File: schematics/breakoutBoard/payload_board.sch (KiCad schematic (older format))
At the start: 10 parts, among them J1 Power_Breakout, J2 MIO_Breakout, J3 USB_OTG_Breakout, J4 Cardedge breakout, P1 CONN_02X50, P2 CONN_02X50, P3 CONN_02X50, P4 CONN_02X50, P5 CONN_02X30, P7 CONN_02X30

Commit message: Fixed gerber files
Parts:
- J1: symbol Conn_01x10 -> conn:Conn_01x10
- J2: symbol Conn_01x12 -> conn:Conn_01x12
- J3: symbol Conn_02x03_Counter_Clockwise -> conn:Conn_02x03_Counter_Clockwise
- J4: symbol Conn_01x17 -> conn:Conn_01x17
- P1, P2, P3, P4: symbol CONN_02X50 -> payload_board-rescue:CONN_02X50
- P5, P7: symbol Conn_02x30_Odd_Even -> conn:Conn_02x30_Odd_Even
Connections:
- wire segments 439 -> 822

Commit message: completed layout w/o impedance matching
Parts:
- removed J1: Power_Breakout, Pin_Headers:Pin_Header_Straight_1x10_Pitch2.54mm, symbol conn:Conn_01x10
- removed J2: MIO_Breakout, Pin_Headers:Pin_Header_Straight_1x12_Pitch2.54mm, symbol conn:Conn_01x12
- removed J3: USB_OTG_Breakout, Pin_Headers:Pin_Header_Straight_1x06_Pitch2.54mm, symbol conn:Conn_02x03_Counter_Clockwise
- removed J4: Cardedge breakout, Pin_Headers:Pin_Header_Straight_1x17_Pitch2.54mm, symbol conn:Conn_01x17
- removed P5: CONN_02X30, Connectors_Samtec:MECF-30-01-L-DV-WT_Socket, symbol conn:Conn_02x30_Odd_Even
- removed P7: CONN_02X30, Connectors_Samtec:MECF-30-0_-NP-L-DV_Edge, symbol conn:Conn_02x30_Odd_Even
- added RIB1: B5B-EH-A, breakoutBoard:B5B-EH-A, symbol payload_board-rescue:B5B-EH-A
- added SMA1: Molex-MMCX-SMD, breakoutBoard:Molex MMCX SMD 50Ohm, symbol payload_board-rescue:Molex-MMCX-SMD
- added U1: breakout_carrier, breakoutBoard:breakout_carrier, symbol payload_board-rescue:breakout_carrier
- P1, P2, P3, P4: footprint Project:BERGSTAK_100_PIN1_RIGHT -> breakoutBoard:BERGSTAK_100_PIN1_RIGHT
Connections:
- net labels removed: +5V, 3V3_I2C, AD9361_GPO_VDD, AUXADC, AUXDAC1, AUXDAC2, Carrier_Reset, FPGA_DONE, FPGA_VBATT, GND, GPO_0, GPO_1, GPO_2, GPO_3, IO_00_33_JX1, IO_L01_33_JX1_N, IO_L01_33_JX1_P, IO_L16_33_JX1_N, IO_L16_33_JX1_P, IO_L18_33_JX1_N, IO_L18_33_JX1_P, IO_L20_33_JX1_N, IO_L20_33_JX1_P, IO_L22_33_JX1_N, IO_L22_33_JX1_P, JTAG_TCK, JTAG_TDI, JTAG_TDO, JTAG_TMS, JX_MGTAVCC, JX_MGTAVTT, JX_VCCO_12, JX_VCCO_13, JX_VCCO_33_34, MIO0, MIO10, MIO11, MIO12, MIO13, MIO14, MIO15, MIO46, MIO47, MIO48, MIO49, MIO51, PG_1P8V, PG_MODULE, PWR_ENABLE, USB_ID, USB_OTG_CPEN, USB_OTG_N, USB_OTG_P, USB_VBUS_OTG, VCCO_13, VDDA_GPO_PWR
- wire segments 822 -> 48
- no-connect marks 4 -> 0
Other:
- note removed: "<-Might need to remove"
- note removed: "JX1\n"
- note removed: "JX2\n"
- note removed: "JX3"
- note removed: "JX4"

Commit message: 'final' push
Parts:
- removed RIB1: B5B-EH-A, breakoutBoard:B5B-EH-A, symbol payload_board-rescue:B5B-EH-A
- added SMA2: Molex-MMCX-SMD, breakoutBoard:Molex MMCX SMD 50Ohm, symbol payload_board-rescue:Molex-MMCX-SMD
- added e1: ribbon2.54mmPitch, breakoutBoard:ribbon2.5mmPitch, symbol payload_board-rescue:ribbon2.54mmPitch
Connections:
- net at P2.17 (P17), U1.1 (SDR_EN): now also e1.2 (I2C_SCL)
- net at P2.19 (P19), U1.2 (UART_TX): now also e1.3 (I2C_SDA)
- net at P1.5 (P5), U1.3 (UART_RX): now also e1.4 (SDR_EN)
- net at P1.57 (P57), P1.58 (P58), P1.59 (P59)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: now also e1.1 (PWR)
- net at P3.11 (P11): now also P1.78 (P78), P1.79 (P79), P1.80 (P80), P1.95 (P95), P2.78 (P78), P2.79 (P79), P2.80 (P80), P2.98 (P98), P3.30 (P30), P3.32 (P32), P3.45 (P45), P3.46 (P46), P3.5 (P5), P3.7 (P7), P3.9 (P9), e1.5 (GND)
- net at P1.92 (P92): no longer SMA1.1 (RF_DIFF+)
- net at P1.94 (P94): no longer SMA1.2 (RF_DIFF-)
- net at P4.98 (P98): now also e1.6 (UART_TX)
- net at P4.99 (P99): now also e1.7 (UART_RX)
- new net: SMA1.1 (RF_DIFF+), SMA2.1 (RF_DIFF+)
- new net: SMA1.2 (RF_DIFF-), SMA2.2 (RF_DIFF-)
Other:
- moved on the sheet: SMA1
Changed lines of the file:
@@
-	1    0    0    -1
-$EndComp
-$Comp
-L payload_board-rescue:B5B-EH-A RIB1
-U 1 1 5CCD2E38
-P 2800 7150
-F 0 "RIB1" H 3078 7079 50  0000 L CNN
-F 1 "B5B-EH-A" H 3078 6988 50  0000 L CNN
-F 2 "breakoutBoard:B5B-EH-A" H 3078 6897 50  0000 L CNN
-F 3 "" H 2750 7250 50  0001 C CNN
-	1    2800 7150
 	1    0    0    -1
 $EndComp
@@
 L payload_board-rescue:Molex-MMCX-SMD SMA1
 U 1 1 5CCDD268
-P 2350 5850
-F 0 "SMA1" H 2428 5713 50  0000 L CNN
-F 1 "Molex-MMCX-SMD" H 2350 6100 50  0001 C CNN
-F 2 "breakoutBoard:Molex MMCX SMD 50Ohm" H 2350 5850 50  0001 C CNN
-F 3 "" H 2350 5850 50  0001 C CNN
-	1    2350 5850
+P 4950 7100
+F 0 "SMA1" H 5028 6963 50  0000 L CNN
+F 1 "Molex-MMCX-SMD" H 4950 7350 50  0001 C CNN
+F 2 "breakoutBoard:Molex MMCX SMD 50Ohm" H 4950 7100 50  0001 C CNN
+F 3 "" H 4950 7100 50  0001 C CNN
+	1    4950 7100
 	0    -1   1    0
 $EndComp
 Wire Wire Line
-	2250 5850 2050 5850
-Wire Wire Line
-	2250 5950 2050 5950
-Wire Wire Line
 	2950 7050 2950 6400
 Wire Wire Line
@@
 Wire Wire Line
 	1400 6400 2950 6400
+Wire Wire Line
+	2200 5150 2050 5150
+Wire Wire Line
+	2050 5250 2200 5250
+Wire Wire Line
+	2200 5250 2200 5150
+Wire Wire Line
+	1550 5250 1250 5250
+Wire Wire Line
+	1250 5250 1250 7550
+Wire Wire Line
+	1250 7550 3250 7550
+Wire Wire Line
+	3250 7550 3250 6400
+Wire Wire Line
+	3250 6400 3100 6400
+Connection ~ 2950 6400
+Wire Wire Line
+	3250 6400 3250 5350
+Wire Wire Line
+	3250 5350 3950 5350
+Connection ~ 3250 6400
+Wire Wire Line
+	4650 5250 5050 5250
+Wire Wire Line
+	5050 5250 5050 5350
+Wire Wire Line
+	5050 6600 3950 6600
+Wire Wire Line
+	3950 6600 3950 5350
+Connection ~ 3950 5350
+Wire Wire Line
+	3950 5350 4150 5350
+Wire Wire Line
+	4650 5350 5050 5350
+Connection ~ 5050 5350
+Wire Wire Line
+	5050 5350 5050 6250
+Wire Wire Line
+	4650 6250 5050 6250
+Connection ~ 5050 6250
+Wire Wire Line
+	5050 6250 5050 6600
+Wire Wire Line
+	7650 3300 7900 3300
+Wire Wire Line
+	7900 3300 7900 3750
+Wire Wire Line
+	7900 3750 6950 3750
+Wire Wire Line
+	5050 3750 5050 5250
+Connection ~ 5050 5250
+Wire Wire Line
+	7150 3300 6950 3300
+Connection ~ 6950 3750
+Wire Wire Line
+	6950 3750 5050 3750
+Wire Wire Line
+	7650 2500 7900 2500
+Wire Wire Line
+	7900 2500 7900 2600
+Connection ~ 7900 3300
+Wire Wire Line
+	7650 2600 7900 2600
+Connection ~ 7900 2600
+Wire Wire Line
+	7900 2600 7900 3300
+Wire Wire Line
+	7150 1300 6950 1300
+Wire Wire Line
+	6950 1300 6950 1400
+Connection ~ 6950 3300
+Wire Wire Line
+	6950 3300 6950 3750
+Wire Wire Line
+	7150 1400 6950 1400
+Connection ~ 6950 1400
+Wire Wire Line
+	6950 1400 6950 1500
+Wire Wire Line
+	7150 1500 6950 1500
+Connection ~ 6950 1500
+Wire Wire Line
+	6950 1500 6950 1600
+Wire Wire Line
+	7150 1600 6950 1600
+Connection ~ 6950 1600
+Wire Wire Line
+	6950 1600 6950 3300
+Wire Wire Line
+	2200 5150 3100 5150
+Wire Wire Line
+	3100 5150 3100 6400
+Connection ~ 2200 5150
+Connection ~ 3100 6400
+Wire Wire Line
+	3100 6400 2950 6400
+$Comp
+L payload_board-rescue:ribbon2.54mmPitch e1
+U 1 1 5CCBC1CC
+P 2700 7250
+F 0 "e1" H 3150 7250 50  0001 C CNN
+F 1 "ribbon2.54mmPitch" H 3228 7213 50  0000 L CNN
+F 2 "breakoutBoard:ribbon2.5mmPitch" H 3150 7250 50  0001 C CNN
+F 3 "" H 3150 7250 50  0001 C CNN
+	1    2700 7250
+	1    0    0    -1
+$EndComp
+$Comp
+L payload_board-rescue:Molex-MMCX-SMD SMA2
+U 1 1 5CCBDC56
+P 4550 7100
+F 0 "SMA2" H 4628 6963 50  0000 L CNN
+F 1 "Molex-MMCX-SMD" H 4550 7350 50  0001 C CNN
+F 2 "breakoutBoard:Molex MMCX SMD 50Ohm" H 4550 7100 50  0001 C CNN
+F 3 "" H 4550 7100 50  0001 C CNN
+	1    4550 7100
+	0    1    1    0
+$EndComp
+Wire Wire Line
+	4650 7100 4850 7100
+Wire Wire Line
+	4850 7200 4650 7200
+Wire Wire Line
+	9750 6300 10300 6300
+Wire Wire Line
+	10300 6300 10300 6700
+Wire Wire Line
+	10300 6700 3050 6700
+Wire Wire Line
+	3050 6700 3050 7050
+Wire Wire Line
+	3150 7050 3400 7050
+Wire Wire Line
+	4200 7050 4200 6850
+Wire Wire Line
+	4200 6850 9100 6850
+Wire Wire Line
+	9100 6850 9100 6400
+Wire Wire Line
+	9100 6400 9250 6400
+Wire Wire Line
+	2150 7250 2400 7250
+Wire Wire Line
+	2400 7250 2400 6700
+Wire Wire Line
+	2400 6700 3050 6700
+Connection ~ 3050 6700
+Wire Wire Line
+	3400 7050 3400 7400
+Wire Wire Line
+	3400 7400 2150 7400
+Connection ~ 3400 7050
+Wire Wire Line
+	3400 7050 4200 7050
 $EndSCHEMATC

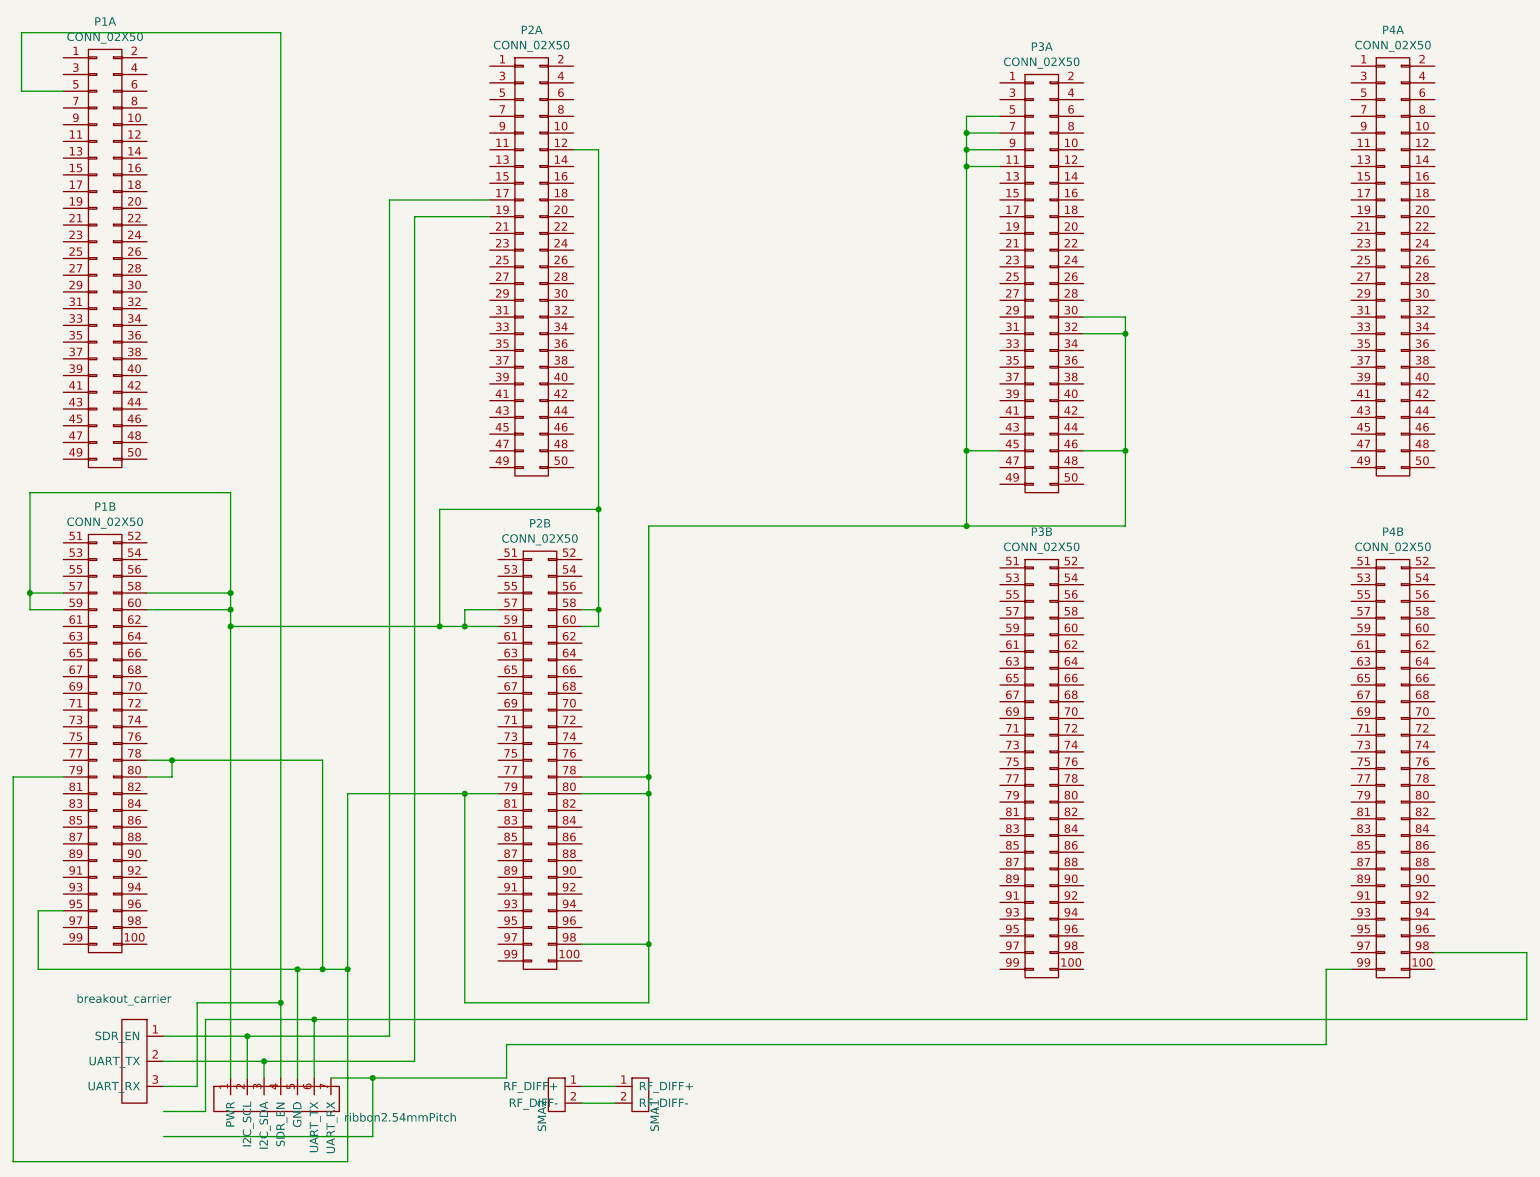
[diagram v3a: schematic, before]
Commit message: final board v2, now with UART
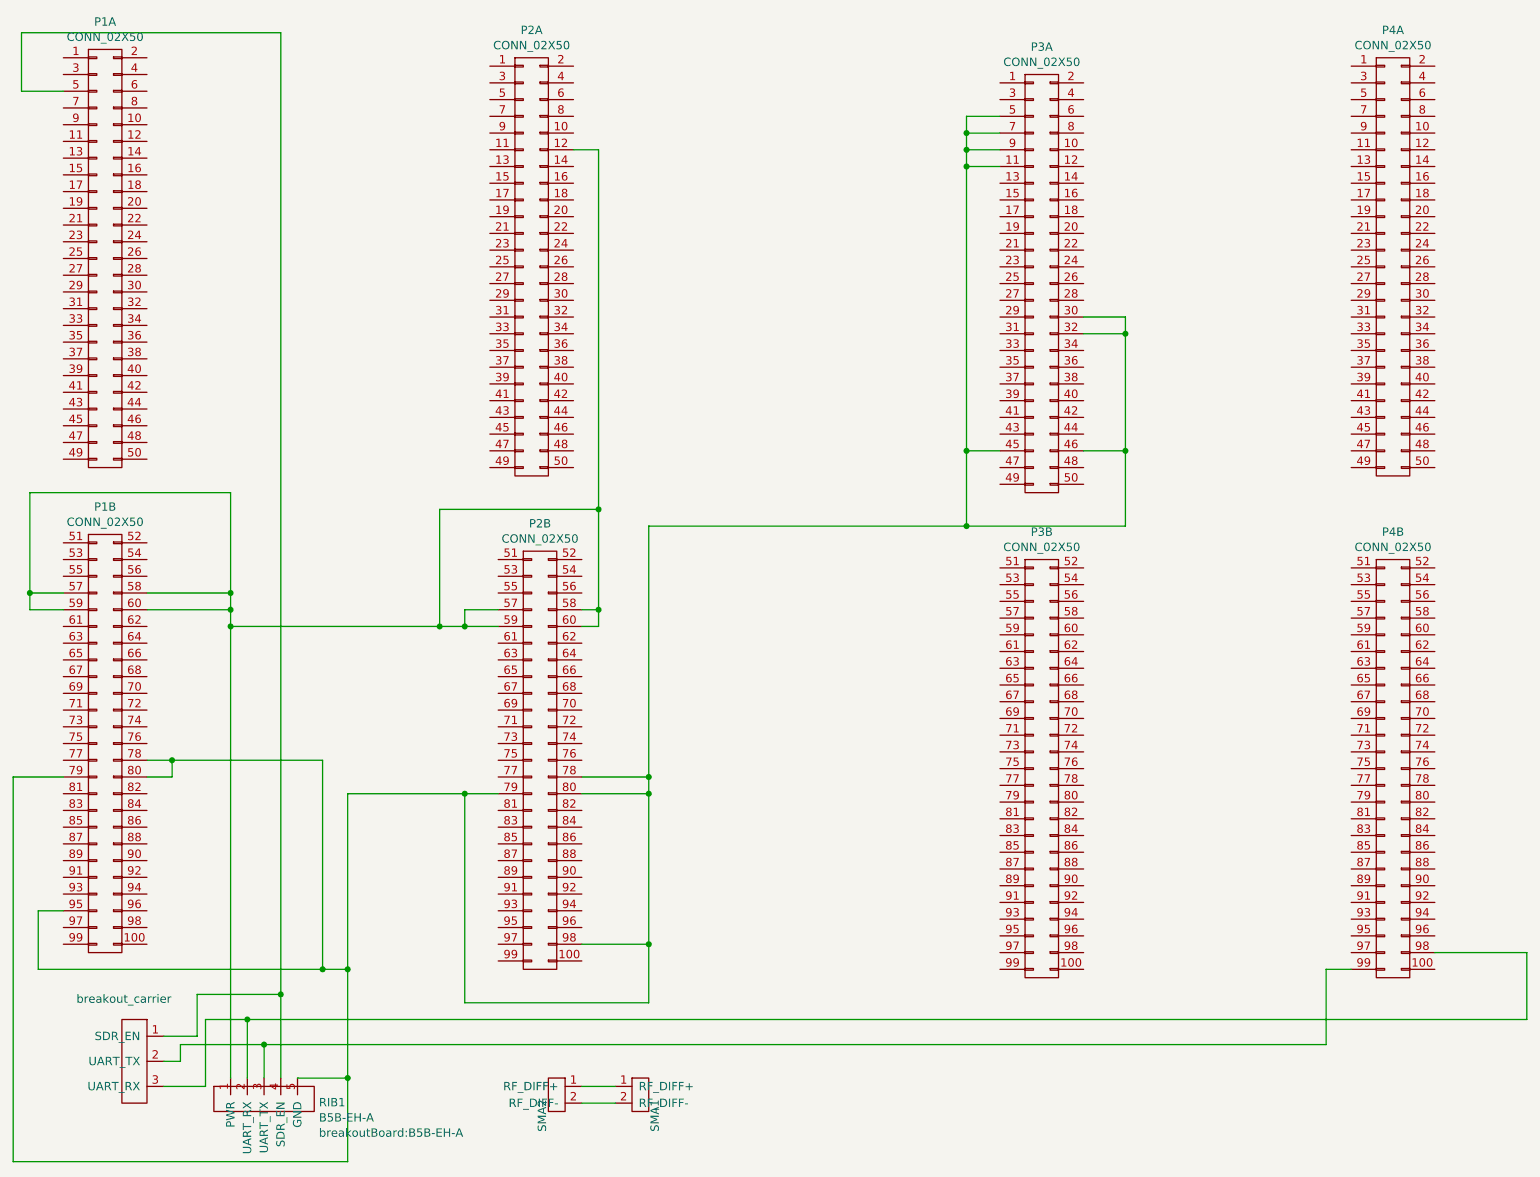
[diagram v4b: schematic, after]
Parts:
- removed e1: ribbon2.54mmPitch, breakoutBoard:ribbon2.5mmPitch, symbol payload_board-rescue:ribbon2.54mmPitch
- added RIB1: B5B-EH-A, breakoutBoard:B5B-EH-A, symbol payload_board-rescue:B5B-EH-A
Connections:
- net at U1.1 (SDR_EN): now also P1.5 (P5), RIB1.4 (SDR_EN); no longer P2.17 (P17)
- net at U1.2 (UART_TX): now also P4.99 (P99), RIB1.3 (UART_TX); no longer P2.19 (P19)
- net at U1.3 (UART_RX): now also P4.98 (P98), RIB1.2 (UART_RX); no longer P1.5 (P5)
- net at P1.57 (P57), P1.58 (P58), P1.59 (P59)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: now also RIB1.1 (PWR)
- net at P1.78 (P78), P1.79 (P79), P1.80 (P80)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: now also RIB1.5 (GND)
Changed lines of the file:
@@
 Wire Wire Line
 	1300 1150 1550 1150
-Wire Wire Line
-	4100 1900 3650 1900
-Wire Wire Line
-	2650 6800 3500 6800
-Wire Wire Line
-	2750 7050 2750 6950
-Wire Wire Line
-	3500 1800 4100 1800
-Wire Wire Line
-	3500 1800 3500 6800
-Wire Wire Line
-	2750 6950 3650 6950
-Wire Wire Line
-	3650 1900 3650 6950
-Wire Wire Line
-	2650 6800 2650 7050
-Wire Wire Line
-	2850 800  2850 6600
 $Comp
 L payload_board-rescue:breakout_carrier U1
@@
 $EndComp
 Wire Wire Line
-	2150 6800 2650 6800
-Connection ~ 2650 6800
-Wire Wire Line
-	2150 6950 2750 6950
-Connection ~ 2750 6950
-Wire Wire Line
-	2150 7100 2350 7100
-Wire Wire Line
-	2350 7100 2350 6600
-Wire Wire Line
-	2350 6600 2850 6600
-Connection ~ 2850 6600
-Wire Wire Line
-	2850 6600 2850 7050
-Wire Wire Line
-	2550 7050 2550 4350
-Wire Wire Line
 	2550 4150 2050 4150
 Wire Wire Line
@@
 Wire Wire Line
 	2550 4350 3800 4350
-Connection ~ 2550 4350
 Wire Wire Line
 	2550 4350 2550 4250
@@
 $EndComp
 Wire Wire Line
-	2950 7050 2950 6400
-Wire Wire Line
 	1400 6400 1400 6050
 Wire Wire Line
 	1400 6050 1550 6050
 Wire Wire Line
-	1400 6400 2950 6400
-Wire Wire Line
 	2200 5150 2050 5150
 Wire Wire Line
@@
 	1250 7550 3250 7550
 Wire Wire Line
-	3250 7550 3250 6400
+	3250 7550 3250 7050
 Wire Wire Line
 	3250 6400 3100 6400
-Connection ~ 2950 6400
 Wire Wire Line
 	3250 6400 3250 5350
@@
 Connection ~ 2200 5150
 Connection ~ 3100 6400
-Wire Wire Line
-	3100 6400 2950 6400
-$Comp
-L payload_board-rescue:ribbon2.54mmPitch e1
-U 1 1 5CCBC1CC
-P 2700 7250
-F 0 "e1" H 3150 7250 50  0001 C CNN
-F 1 "ribbon2.54mmPitch" H 3228 7213 50  0000 L CNN
-F 2 "breakoutBoard:ribbon2.5mmPitch" H 3150 7250 50  0001 C CNN
-F 3 "" H 3150 7250 50  0001 C CNN
-	1    2700 7250
-	1    0    0    -1
-$EndComp
 $Comp
 L payload_board-rescue:Molex-MMCX-SMD SMA2
@@
 	10300 6300 10300 6700
 Wire Wire Line
-	10300 6700 3050 6700
-Wire Wire Line
-	3050 6700 3050 7050
-Wire Wire Line
-	3150 7050 3400 7050
-Wire Wire Line
-	4200 7050 4200 6850
-Wire Wire Line
-	4200 6850 9100 6850
-Wire Wire Line
 	9100 6850 9100 6400
 Wire Wire Line
 	9100 6400 9250 6400
-Wire Wire Line
-	2150 7250 2400 7250
-Wire Wire Line
-	2400 7250 2400 6700
-Wire Wire Line
-	2400 6700 3050 6700
-Connection ~ 3050 6700
-Wire Wire Line
-	3400 7050 3400 7400
-Wire Wire Line
-	3400 7400 2150 7400
-Connection ~ 3400 7050
-Wire Wire Line
-	3400 7050 4200 7050
+$Comp
+L payload_board-rescue:B5B-EH-A RIB1
+U 1 1 5CCD5DF0
+P 2800 7150
+F 0 "RIB1" H 3078 7104 50  0000 L CNN
+F 1 "B5B-EH-A" H 3078 7013 50  0000 L CNN
+F 2 "breakoutBoard:B5B-EH-A" H 3078 6922 50  0000 L CNN
+F 3 "" H 2750 7250 50  0001 C CNN
+	1    2800 7150
+	1    0    0    -1
+$EndComp
+Connection ~ 2550 4350
+Wire Wire Line
+	2550 7050 2550 4350
+Wire Wire Line
+	1400 6400 3100 6400
+Wire Wire Line
+	2400 6700 2650 6700
+Wire Wire Line
+	2950 7050 3250 7050
+Connection ~ 3250 7050
+Wire Wire Line
+	3250 7050 3250 6400
+Wire Wire Line
+	2650 6700 2650 7050
+Connection ~ 2650 6700
+Wire Wire Line
+	2650 6700 10300 6700
+Wire Wire Line
+	2750 6850 2750 7050
+Wire Wire Line
+	2850 800  2850 6550
+Wire Wire Line
+	2150 7100 2400 7100
+Wire Wire Line
+	2400 7100 2400 6700
+Wire Wire Line
+	2150 6950 2250 6950
+Wire Wire Line
+	2250 6950 2250 6850
+Wire Wire Line
+	2250 6850 2750 6850
+Connection ~ 2750 6850
+Wire Wire Line
+	2150 6800 2350 6800
+Wire Wire Line
+	2350 6800 2350 6550
+Wire Wire Line
+	2350 6550 2850 6550
+Connection ~ 2850 6550
+Wire Wire Line
+	2850 6550 2850 7050
+Wire Wire Line
+	2750 6850 9100 6850
 $EndSCHEMATC
